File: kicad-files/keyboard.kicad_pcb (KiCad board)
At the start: 2 copper layers, 349.5 x 100 mm, 187 parts, among them J1 TYPE-C-31-M12_13, Q1 2N7002, Q2 2N7002, SW1 K2-1187SQ-A4SW-06, T1 53261-0471, T2 53261-0471, U1 STM32F411CEU6, U2 USBLC6-2SC6, U3 AT24C256C-SSHL-T, U4 SGM2007-3.3XN5/TR, Y1 TAXM8M4RFDCET2T

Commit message: Straightened up the daughter board
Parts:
- moved F1 0.50 mm to (347.5, 48.0)
- moved T1 0.27 mm to (342.7, 58.1)
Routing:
- net Net-(T1-D+): track 8.93 -> 8.43 mm
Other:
- board size 349.5 x 100 mm -> 350.2 x 100 mm
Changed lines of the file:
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@@
   )
   (footprint "Fuse:Fuse_1206_3216Metric" (layer "F.Cu")
-    (at 347 48 -90)
+    (at 347.5 48 -90)
     (descr "Fuse SMD 1206 (3216 Metric), square (rectangular) end terminal, IPC_7351 nominal, (Body size source: http://www.tortai-tech.com/upload/download/2011102023233369053.pdf), generated with kicad-footprint-generator")
     (tags "fuse")
@@
   )
   (footprint "Legshark:Molex, PicoBlade, 53261, 4 Way, 1 Row, Right Angle PCB Header" (layer "F.Cu")
-    (at 342.5 58.275)
+    (at 342.7 58.1)
     (property "Sheetfile" "keyboard.kicad_sch")
     (property "Sheetname" "")
@@
       (polygon
         (pts
-          (xy 336.7 58.275)
-          (xy 348.2 58.275)
-          (xy 348.2 62.175)
-          (xy 336.7 62.175)
+          (xy 336.9 58.1)
+          (xy 348.4 58.1)
+          (xy 348.4 62)
+          (xy 336.9 62)
         )
       )
@@
   (gr_rect (start 302.25 52.75) (end 312.25 63)
     (stroke (width 0.15) (type dash)) (fill none) (layer "B.SilkS"))
-  (gr_rect (start 344.744268 44.077568) (end 349.34334 52.23922)
+  (gr_rect (start 345.244268 44.077568) (end 349.34334 52.23922)
     (stroke (width 0.15) (type solid)) (fill none) (layer "F.SilkS"))
+  (gr_line (start 342.7 42.8) (end 342.7 63.5)
+    (stroke (width 0.1) (type default)) (layer "Eco1.User"))
   (gr_line locked (start 0 50) (end 325 50)
     (stroke (width 0.5) (type default)) (layer "Eco1.User"))
   (gr_line locked (start 162.5 0) (end 162.5 100)
     (stroke (width 0.5) (type default)) (layer "Eco1.User"))
+  (gr_line (start 335.2 61) (end 335.2 36)
+    (stroke (width 0.1) (type default)) (layer "Edge.Cuts"))
+  (gr_line (start 336.2 35) (end 349.2 35)
+    (stroke (width 0.1) (type default)) (layer "Edge.Cuts"))
+  (gr_line (start 349.2 62) (end 336.2 62)
+    (stroke (width 0.1) (type default)) (layer "Edge.Cuts"))
+  (gr_arc (start 335.2 36) (mid 335.492893 35.292893) (end 336.2 35)
+    (stroke (width 0.1) (type default)) (layer "Edge.Cuts"))
   (gr_arc (start 5 100) (mid 1.464467 98.535534) (end 0 95)
     (stroke (width 0.5) (type default)) (layer "Edge.Cuts"))
+  (gr_arc (start 336.2 62) (mid 335.492893 61.707107) (end 335.2 61)
+    (stroke (width 0.1) (type default)) (layer "Edge.Cuts"))
+  (gr_line (start 350.2 36) (end 350.2 61)
+    (stroke (width 0.1) (type default)) (layer "Edge.Cuts"))
+  (gr_arc (start 350.2 61) (mid 349.907107 61.707107) (end 349.2 62)
+    (stroke (width 0.1) (type default)) (layer "Edge.Cuts"))
   (gr_arc (start 325 95) (mid 323.535534 98.535533) (end 320 100)
     (stroke (width 0.5) (type default)) (layer "Edge.Cuts"))
   (gr_line (start 325 5) (end 325 95)
     (stroke (width 0.5) (type default)) (layer "Edge.Cuts"))
-  (gr_rect (start 335.5 35) (end 349.5 62)
-    (stroke (width 0.1) (type default)) (fill none) (layer "Edge.Cuts"))
   (gr_line (start 5 0) (end 320 0)
     (stroke (width 0.5) (type default)) (layer "Edge.Cuts"))
@@
   (gr_line (start 0 95) (end 0 5)
     (stroke (width 0.5) (type default)) (layer "Edge.Cuts"))
+  (gr_arc (start 349.2 35) (mid 349.907107 35.292893) (end 350.2 36)
+    (stroke (width 0.1) (type default)) (layer "Edge.Cuts"))
   (gr_text "HARD RESET" (at 311.75 55.25) (layer "B.SilkS")
     (effects (font (size 1 1) (thickness 0.15)) (justify left bottom mirror))
@@
   (segment (start 340.75 49.4) (end 338.95 47.6) (width 0.5) (layer "F.Cu") (net 111))
   (segment (start 338.52 48.48) (end 337.23 48.48) (width 0.5) (layer "F.Cu") (net 111))
-  (segment (start 347.5 49.4) (end 344.75 49.4) (width 0.5) (layer "F.Cu") (net 111))
   (segment (start 343.05146 49.4) (end 340.75 49.4) (width 0.5) (layer "F.Cu") (net 111))
   (segment (start 338.95 47.5) (end 338.95 48.05) (width 0.5) (layer "F.Cu") (net 111))
@@
   (segment (start 338.95 48.05) (end 338.52 48.48) (width 0.5) (layer "F.Cu") (net 111))
   (segment (start 343.885806 51.718694) (end 343.885806 49.459497) (width 0.5) (layer "F.Cu") (net 111))
-  (segment (start 344.75 49.4) (end 343.05146 49.4) (width 0.5) (layer "F.Cu") (net 111))
   (segment (start 337.05 48.3) (end 337.05 47.5) (width 0.5) (layer "F.Cu") (net 111))
+  (segment (start 343.05146 49.4) (end 347.5 49.4) (width 0.5) (layer "F.Cu") (net 111))
   (segment (start 338.778422 51.864636) (end 338.778422 51.428422) (width 0.5) (layer "F.Cu") (net 113))
   (segment (start 338.778422 51.428422) (end 337.05 49.7) (width 0.5) (layer "F.Cu") (net 113))
@@
   (segment (start 311.675 66.425) (end 313.25 64.85) (width 0.25) (layer "B.Cu") (net 123))
   (segment (start 309.425 66.425) (end 311.675 66.425) (width 0.25) (layer "B.Cu") (net 123))
-  (segment (start 345.15 43.5) (end 345.15 44.25) (width 0.5) (layer "F.Cu") (net 124))
   (segment (start 345.15 44.25) (end 347.5 46.6) (width 0.5) (layer "F.Cu") (net 124))
+  (segment (start 345.15 43.5) (end 345.15 44.25) (width 0.5) (layer "F.Cu") (net 124))
   (segment (start 340.25 42.0725) (end 340.25 44) (width 0.5) (layer "F.Cu") (net 124))
   (segment (start 345.15 42.0725) (end 345.15 43.5) (width 0.5) (layer "F.Cu") (net 124))
@@
   (segment (start 269.340069 68.416315) (end 272.854919 68.416315) (width 0.25) (layer "B.Cu") (net 152))
   (segment (start 267.3 52.55) (end 265.65 50.9) (width 0.25) (layer "B.Cu") (net 152))
-  (segment (start 340.585806 51.718694) (end 340.585806 57.460806) (width 0.5) (layer "F.Cu") (net 154))
+  (segment (start 340.7 51.718694) (end 340.7 57.460806) (width 0.5) (layer "F.Cu") (net 154))
   (segment (start 340.585806 51.718694) (end 340.585806 51.335806) (width 0.5) (layer "F.Cu") (net 154))
   (segment (start 340.585806 51.335806) (end 338.95 49.7) (width 0.5) (layer "F.Cu") (net 154))
-  (segment (start 340.585806 57.460806) (end 340.6 57.475) (width 0.5) (layer "F.Cu") (net 154))
-  (segment (start 342.013006 53.987701) (end 343.1 55.074695) (width 0.25) (layer "F.Cu") (net 155))
-  (segment (start 343.1 55.074695) (end 343.1 57.475) (width 0.25) (layer "F.Cu") (net 155))
-  (segment (start 341.987701 53.987701) (end 342.013006 53.987701) (width 0.25) (layer "F.Cu") (net 155))
-  (via (at 341.987701 53.987701) (size 0.8) (drill 0.4) (layers "F.Cu" "B.Cu") (free) (net 155))
-  (segment (start 339.395 50.4) (end 339.3 50.305) (width 0.25) (layer "B.Cu") (net 155))
-  (segment (start 341.438604 50.4) (end 339.395 50.4) (width 0.25) (layer "B.Cu") (net 155))
-  (segment (start 341.987701 53.987701) (end 341.987701 50.949097) (width 0.25) (layer "B.Cu") (net 155))
+  (segment (start 343.077016 57.452016) (end 343.1 57.475) (width 0.25) (layer "F.Cu") (net 155))
+  (segment (start 343.2 54.454798) (end 343.2 57.452016) (width 0.25) (layer "F.Cu") (net 155))
+  (via (at 343.2 54.454798) (size 0.8) (drill 0.4) (layers "F.Cu" "B.Cu") (free) (net 155))
+  (segment (start 343.077016 54.454798) (end 341.770772 54.454798) (width 0.25) (layer "B.Cu") (net 155))
   (segment (start 339.3 50.305) (end 339.3 49.525) (width 0.25) (layer "B.Cu") (net 155))
-  (segment (start 341.987701 50.949097) (end 341.438604 50.4) (width 0.25) (layer "B.Cu") (net 155))
-  (segment (start 342 55) (end 342 57.325) (width 0.25) (layer "F.Cu") (net 156))
+  (segment (start 341.05 52.055) (end 339.3 50.305) (width 0.25) (layer "B.Cu") (net 155))
+  (segment (start 341.05 53.734026) (end 341.05 52.055) (width 0.25) (layer "B.Cu") (net 155))
+  (segment (start 341.770772 54.454798) (end 341.05 53.734026) (width 0.25) (layer "B.Cu") (net 155))
+  (segment (start 341.815833 57.440833) (end 341.85 57.475) (width 0.25) (layer "F.Cu") (net 156))
+  (segment (start 341.9 53.474554) (end 341.9 57.440833) (width 0.25) (layer "F.Cu") (net 156))
   (segment (start 342 57.325) (end 341.85 57.475) (width 0.25) (layer "F.Cu") (net 156))
-  (via (at 342 55) (size 0.8) (drill 0.4) (layers "F.Cu" "B.Cu") (free) (net 156))
-  (segment (start 342.712701 54.287299) (end 342.712701 53.687396) (width 0.25) (layer "B.Cu") (net 156))
-  (segment (start 342.5 50.825) (end 341.2 49.525) (width 0.25) (layer "B.Cu") (net 156))
-  (segment (start 342.5 53.474695) (end 342.5 50.825) (width 0.25) (layer "B.Cu") (net 156))
-  (segment (start 342 55) (end 342.712701 54.287299) (width 0.25) (layer "B.Cu") (net 156))
-  (segment (start 342.712701 53.687396) (end 342.5 53.474695) (width 0.25) (layer "B.Cu") (net 156))
+  (via (at 341.9 53.474554) (size 0.8) (drill 0.4) (layers "F.Cu" "B.Cu") (free) (net 156))
+  (segment (start 341.815833 53.474554) (end 341.5 53.158721) (width 0.25) (layer "B.Cu") (net 156))
+  (segment (start 341.5 49.825) (end 341.2 49.525) (width 0.25) (layer "B.Cu") (net 156))
+  (segment (start 341.5 53.158721) (end 341.5 49.825) (width 0.25) (layer "B.Cu") (net 156))
   (zone (net 104) (net_name "GND") (layer "F.Cu") (hatch edge 0.5)
     (connect_pads (clearance 0.508))
@@
     (connect_pads (clearance 0.508))
     (min_thickness 0.25) (filled_areas_thickness no)
-    (fill yes (thermal_gap 0.5) (thermal_bridge_width 0.5))
+    (fill (thermal_gap 0.5) (thermal_bridge_width 0.5))
     (polygon
       (pts
-        (xy 336.75 35.175)
-        (xy 348.5 35.175)
-        (xy 348.5 42.175)
-        (xy 336.75 42.175)
+        (xy 335 34.5)
+        (xy 350.5 34.5)
+        (xy 350.5 41.5)
+        (xy 335 41.5)
       )
     )

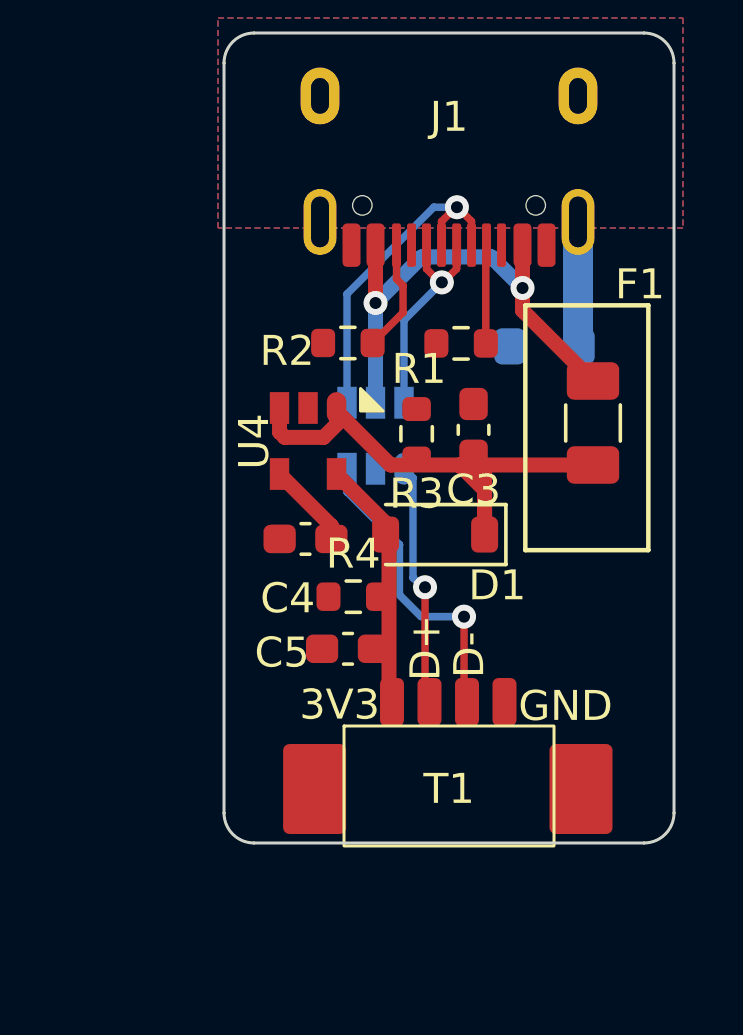
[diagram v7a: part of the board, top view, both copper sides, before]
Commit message: Completed wiring and zoning daughter board
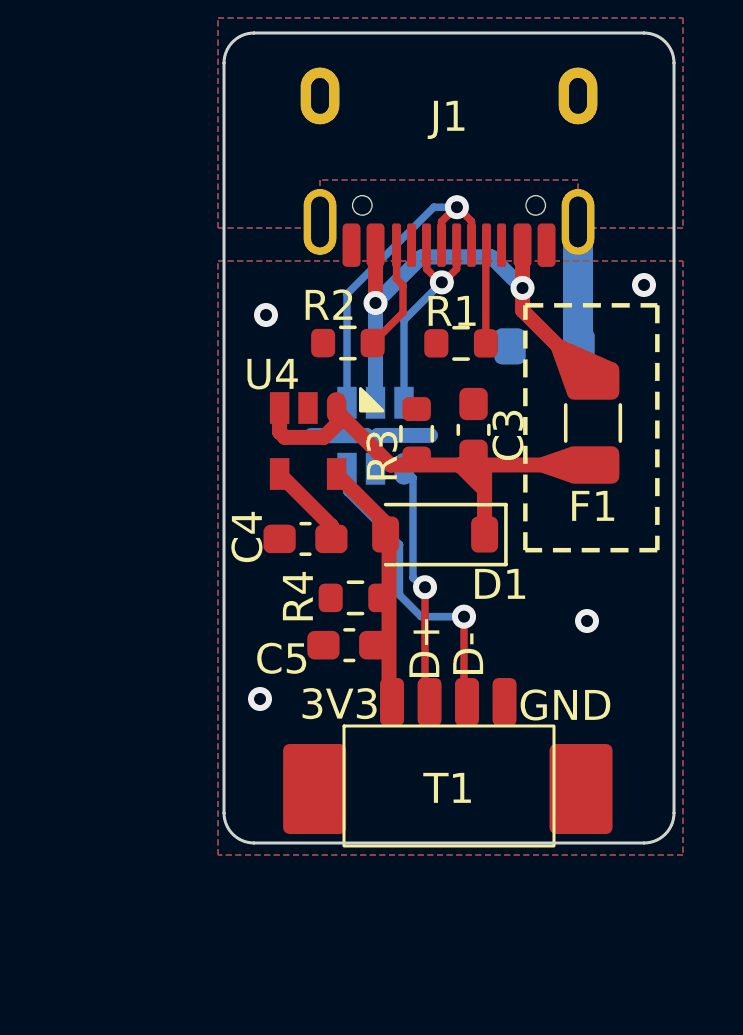
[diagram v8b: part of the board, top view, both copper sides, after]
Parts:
- moved C5 0.13 mm to (339.4, 55.4)
- moved R4 0.08 mm to (339.6, 53.8)
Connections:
- T1 pad : (no net) -> GND1
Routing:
- net GND1: track 0.00 -> 5.98 mm, vias 0 -> 4
- added copper zone on B.Cu, net GND1
- added copper zone on F.Cu, net GND1
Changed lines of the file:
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@@
     )
     (pad_to_mask_clearance 0)
+    (grid_origin 354.5 40.1)
     (pcbplotparams
       (layerselection 0x00010fc_ffffffff)
@@
     (property "ki_keywords" "cap capacitor")
     (attr smd)
-    (fp_text reference "C4" (at 0.592256 -1.980766) (layer "F.SilkS")
+    (fp_text reference "C4" (at 1.915922 0.064636 90) (layer "F.SilkS")
         (effects (font (size 1 1) (thickness 0.15)))
     )
@@
   )
   (footprint "Capacitor_SMD:C_0603_1608Metric_Pad1.08x0.95mm_HandSolder" (layer "F.Cu")
-    (at 339.332802 55.526168 180)
+    (at 339.37744 55.405781 180)
     (descr "Capacitor SMD 0603 (1608 Metric), square (rectangular) end terminal, IPC_7351 nominal with elongated pad for handsoldering. (Body size source: IPC-SM-782 page 76, https://www.pcb-3d.com/wordpress/wp-content/uploads/ipc-sm-782a_amendment_1_and_2.pdf), generated with kicad-footprint-generator")
     (tags "capacitor handsolder")
@@
     (property "ki_keywords" "cap capacitor")
     (attr smd)
-    (fp_text reference "C5" (at 2.19886 -0.128915) (layer "F.SilkS")
+    (fp_text reference "C5" (at 2.232802 -0.473832) (layer "F.SilkS")
         (effects (font (size 1 1) (thickness 0.15)))
     )
@@
     (property "ki_keywords" "R res resistor")
     (attr smd)
-    (fp_text reference "R1" (at 1.401352 -0.853804) (layer "F.SilkS")
+    (fp_text reference "R1" (at 0.301352 1.046196) (layer "F.SilkS")
         (effects (font (size 1 1) (thickness 0.15)))
     )
@@
     (property "ki_keywords" "fuse")
     (attr smd)
-    (fp_text reference "F1" (at -4.621285 -1.564218) (layer "F.SilkS")
+    (fp_text reference "F1" (at 2.8 0) (layer "F.SilkS")
         (effects (font (size 1 1) (thickness 0.15)))
     )
@@
     (property "ki_keywords" "cap capacitor")
     (attr smd)
-    (fp_text reference "C3" (at -2 0 180) (layer "F.SilkS")
+    (fp_text reference "C3" (at -0.171145 1.182336 270) (layer "F.SilkS")
         (effects (font (size 1 1) (thickness 0.15)))
     )
@@
     (pad "" smd roundrect (at -4.48 2.1 90) (size 3 2.1) (layers "F.Cu" "F.Paste" "F.Mask") (roundrect_rratio 0.1)
       (chamfer_ratio 0.05) (chamfer)
-      (thermal_bridge_angle 45))
+      (net 153 "GND1") (thermal_bridge_angle 45))
     (pad "" smd roundrect (at 4.4 2.1 90) (size 3 2.1) (layers "F.Cu" "F.Paste" "F.Mask") (roundrect_rratio 0.1)
       (chamfer_ratio 0.05) (chamfer)
-      (thermal_bridge_angle 45))
+      (net 153 "GND1") (thermal_bridge_angle 45))
     (pad "1" smd roundrect (at -1.9 -0.8 90) (size 1.6 0.8) (layers "F.Cu" "F.Paste" "F.Mask") (roundrect_rratio 0.25)
       (net 154 "Net-(D1-A)") (pinfunction "3V3") (pintype "input") (thermal_bridge_angle 45))
@@
     (property "ki_keywords" "R res resistor")
     (attr smd)
-    (fp_text reference "R2" (at 2.028751 -0.265966) (layer "F.SilkS")
+    (fp_text reference "R2" (at 0.628751 1.234034) (layer "F.SilkS")
         (effects (font (size 1 1) (thickness 0.15)))
     )
@@
     (property "ki_description" "300mA, Low Power, Low Dropout Linear Regulators")
     (attr smd)
-    (fp_text reference "U4" (at 0.017029 1.796439 90) (layer "F.SilkS")
+    (fp_text reference "U4" (at -2.2 1.2 -180) (layer "F.SilkS")
         (effects (font (size 1 1) (thickness 0.2)))
     )
@@
     (property "ki_keywords" "diode Schottky")
     (attr smd)
-    (fp_text reference "D1" (at -2.071187 -1.696179) (layer "F.SilkS")
+    (fp_text reference "D1" (at -2.164194 -1.681306) (layer "F.SilkS")
         (effects (font (size 1 1) (thickness 0.15)))
     )
@@
     (property "ki_keywords" "R res resistor")
     (attr smd)
-    (fp_text reference "R3" (at 2 0 -180) (layer "F.SilkS")
+    (fp_text reference "R3" (at 0.739797 1.120418 -90) (layer "F.SilkS")
         (effects (font (size 1 1) (thickness 0.15)))
     )
@@
   )
   (footprint "Resistor_SMD:R_0603_1608Metric" (layer "F.Cu")
-    (at 339.507932 53.789458)
+    (at 339.581759 53.829607)
     (descr "Resistor SMD 0603 (1608 Metric), square (rectangular) end terminal, IPC_7351 nominal, (Body size source: IPC-SM-782 page 72, https://www.pcb-3d.com/wordpress/wp-content/uploads/ipc-sm-782a_amendment_1_and_2.pdf), generated with kicad-footprint-generator")
     (tags "resistor")
@@
     (property "ki_keywords" "R res resistor")
     (attr smd)
-    (fp_text reference "R4" (at 0 -1.43) (layer "F.SilkS")
+    (fp_text reference "R4" (at -1.881759 -0.029607 90) (layer "F.SilkS")
         (effects (font (size 1 1) (thickness 0.15)))
     )
@@
   (gr_poly
     (pts
+      (xy 346.483072 45.229736)
+      (xy 348.281943 46.025391)
+      (xy 346.644509 47.063201)
+      (xy 346.099659 45.532431)
+      (xy 346.29569 45.362345)
+    )
+    (stroke (width 0) (type solid)) (fill solid) (layer "F.Cu"))
+  (gr_poly
+    (pts
+      (xy 345.74147 49.14819)
+      (xy 346.826847 48.771984)
+      (xy 346.826847 50.017356)
+      (xy 345.74147 49.64115)
+      (xy 345.74147 49.360076)
+    )
+    (stroke (width 0) (type solid)) (fill solid) (layer "F.Cu"))
+  (gr_poly
+    (pts
       (xy 281.741994 70.568458)
       (xy 282.82702 70.633043)
@@
   (gr_rect (start 302.25 52.75) (end 312.25 63)
     (stroke (width 0.15) (type dash)) (fill none) (layer "B.SilkS"))
-  (gr_rect (start 345.244268 44.077568) (end 349.34334 52.23922)
-    (stroke (width 0.15) (type solid)) (fill none) (layer "F.SilkS"))
+  (gr_rect (start 345.244268 44.077568) (end 349.64334 52.23922)
+    (stroke (width 0.15) (type dash)) (fill none) (layer "F.SilkS"))
   (gr_line (start 342.7 42.8) (end 342.7 63.5)
     (stroke (width 0.1) (type default)) (layer "Eco1.User"))
@@
   (segment (start 269.340069 68.416315) (end 272.854919 68.416315) (width 0.25) (layer "B.Cu") (net 152))
   (segment (start 267.3 52.55) (end 265.65 50.9) (width 0.25) (layer "B.Cu") (net 152))
+  (via (at 347.3 54.6) (size 0.8) (drill 0.4) (layers "F.Cu" "B.Cu") (free) (net 153))
+  (via (at 336.6 44.4) (size 0.8) (drill 0.4) (layers "F.Cu" "B.Cu") (free) (net 153))
+  (via (at 336.4 57.2) (size 0.8) (drill 0.4) (layers "F.Cu" "B.Cu") (free) (net 153))
+  (via (at 349.2 43.4) (size 0.8) (drill 0.4) (layers "F.Cu" "B.Cu") (free) (net 153))
+  (segment (start 340.25 48.495) (end 340.330584 48.414416) (width 0.5) (layer "B.Cu") (net 153))
+  (segment (start 340.25 49.525) (end 340.25 48.72) (width 0.5) (layer "B.Cu") (net 153))
+  (segment (start 340.25 49.525) (end 340.25 48.495) (width 0.5) (layer "B.Cu") (net 153))
+  (segment (start 340.25 48.72) (end 339.950903 48.420903) (width 0.5) (layer "B.Cu") (net 153))
+  (segment (start 340.330584 48.414416) (end 342.083289 48.414416) (width 0.5) (layer "B.Cu") (net 153))
+  (segment (start 339.950903 48.420903) (end 338.1 48.420903) (width 0.5) (layer "B.Cu") (net 153))
   (segment (start 340.7 51.718694) (end 340.7 57.460806) (width 0.5) (layer "F.Cu") (net 154))
   (segment (start 340.585806 51.718694) (end 340.585806 51.335806) (width 0.5) (layer "F.Cu") (net 154))
@@
     )
   )
+  (zone (net 153) (net_name "GND1") (layers "F&B.Cu") (hatch edge 0.5)
+    (priority 3)
+    (connect_pads yes (clearance 0.508))
+    (min_thickness 0.25) (filled_areas_thickness no)
+    (fill (thermal_gap 0.2) (thermal_bridge_width 0.8))
+    (polygon
+      (pts
+        (xy 335 42.6)
+        (xy 350.5 42.6)
+        (xy 350.5 62.4)
+        (xy 335 62.4)
+      )
+    )
+  )
   (zone (net 108) (net_name "GNDPWR") (layers "F&B.Cu") (hatch edge 0.5)
     (priority 2)
-    (connect_pads (clearance 0.508))
+    (connect_pads yes (clearance 0.508))
     (min_thickness 0.25) (filled_areas_thickness no)
     (fill (thermal_gap 0.5) (thermal_bridge_width 0.5))
     (polygon
       (pts
-        (xy 335 34.5)
-        (xy 350.5 34.5)
         (xy 350.5 41.5)
+        (xy 347 41.5)
+        (xy 347 39.9)
+        (xy 338.4 39.9)
+        (xy 338.4 41.5)
         (xy 335 41.5)
+        (xy 335 34.5)
+        (xy 350.5 34.5)
       )
     )
